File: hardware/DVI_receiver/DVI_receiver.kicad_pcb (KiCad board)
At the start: 4 copper layers, 43 x 25.8 mm, 59 parts, among them J1 HDMI_A, J2 Conn_01x05_Pin, J6 DF12NB(3.0)-30DS-0.5V(51), J7 DF12NB(3.0)-30DS-0.5V(51), Q1 BSS138, U1 TXS0102DCUR, U5 AMS1117-3.3, U8 TFP401

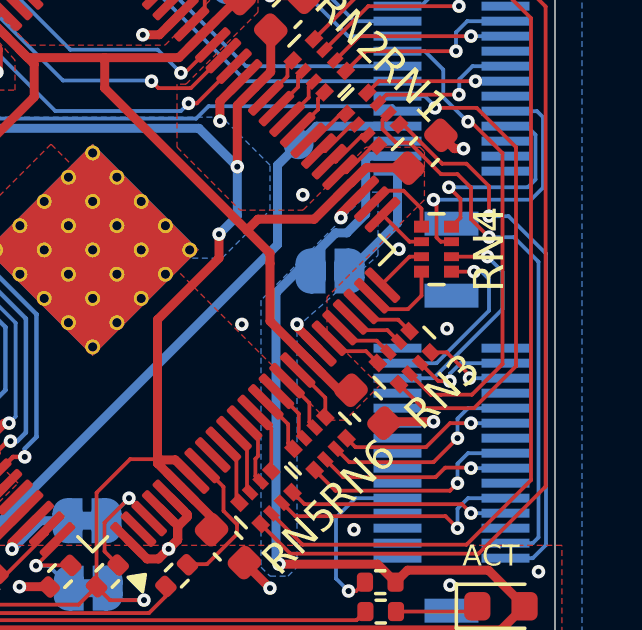
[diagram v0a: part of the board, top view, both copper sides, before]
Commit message: fixed mixup of pins G5/G4 (3rd diff pair ODD) and DE/PCLK (3rd diff pair EVEN), now with correct polarity for diff pairs
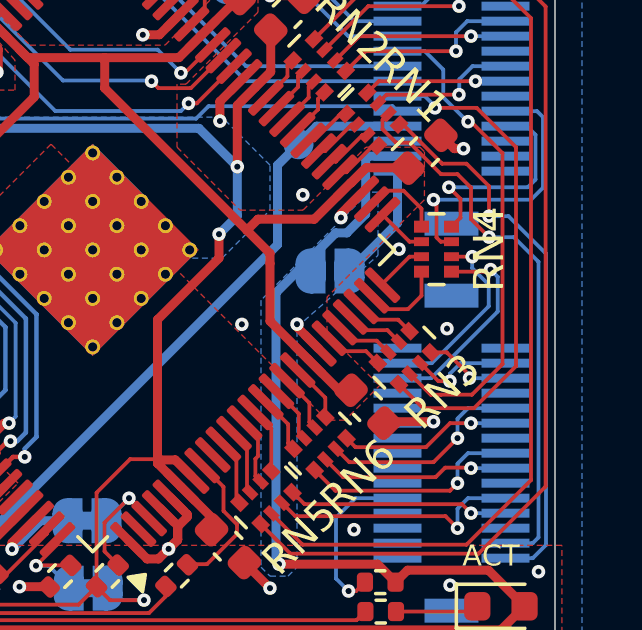
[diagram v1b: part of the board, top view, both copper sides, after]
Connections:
- J6 pad 4: G4 -> G5
- J6 pad 6: G5 -> G4
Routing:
- net G5: track 7.61 -> 6.40 mm
- net G4: track 6.18 -> 7.09 mm
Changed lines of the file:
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@@
 			)
 		)
+		(sheetname "fpga")
+		(sheetfile "fpga.kicad_sch")
 		(attr smd)
 		(fp_line
@@
 			(net 60 "unconnected-(J6-1-Pad2)")
 			(pinfunction "1")
-			(pintype "passive+no_connect")
+			(pintype "passive")
 		)
 		(pad "3" smd rect
@@
 			(size 0.3 1.6)
 			(layers "B.Cu" "B.Paste" "B.Mask")
-			(net 46 "G4")
+			(net 41 "G5")
 			(pinfunction "3")
 			(pintype "passive")
@@
 			(size 0.3 1.6)
 			(layers "B.Cu" "B.Paste" "B.Mask")
-			(net 41 "G5")
+			(net 46 "G4")
 			(pinfunction "5")
 			(pintype "passive")
@@
 	)
 	(segment
-		(start 150.210155 94.319997)
+		(start 149.7 94.319997)
 		(end 149.010155 94.319997)
 		(width 0.127)
@@
 	)
 	(via
-		(at 150.210155 94.319997)
+		(at 149.7 94.319997)
 		(size 0.45)
 		(drill 0.2)
@@
 	)
 	(segment
-		(start 150.710155 96.069998)
-		(end 148.410155 98.369998)
+		(start 150.25 95.975)
+		(end 148.355002 97.869998)
 		(width 0.127)
 		(layer "B.Cu")
@@
 	)
 	(segment
-		(start 150.210155 94.319997)
-		(end 150.710155 94.819996)
+		(start 149.7 94.319997)
+		(end 149.7 94.70191)
 		(width 0.127)
 		(layer "B.Cu")
@@
 	)
 	(segment
-		(start 150.710155 94.819996)
-		(end 150.710155 96.069998)
+		(start 149.7 94.70191)
+		(end 150.25 95.25191)
 		(width 0.127)
 		(layer "B.Cu")
@@
 	)
 	(segment
-		(start 148.410155 98.369998)
-		(end 147.210155 98.369997)
+		(start 148.355002 97.869998)
+		(end 147.210155 97.869998)
+		(width 0.127)
+		(layer "B.Cu")
+		(net 41)
+	)
+	(segment
+		(start 150.25 95.25191)
+		(end 150.25 95.975)
 		(width 0.127)
 		(layer "B.Cu")
@@
 	)
 	(segment
-		(start 149.760156 94.819998)
+		(start 150.241657 94.819998)
 		(end 149.010153 94.819998)
 		(width 0.127)
@@
 		(net 46)
 	)
+	(segment
+		(start 150.311655 94.75)
+		(end 150.241657 94.819998)
+		(width 0.127)
+		(layer "F.Cu")
+		(net 46)
+	)
 	(via
-		(at 149.760156 94.819998)
+		(at 150.311655 94.75)
 		(size 0.45)
 		(drill 0.2)
@@
 	)
 	(segment
-		(start 150.010155 94.819998)
-		(end 150.260155 95.069997)
-		(width 0.127)
-		(layer "B.Cu")
-		(net 46)
-	)
-	(segment
-		(start 149.760156 94.819998)
-		(end 150.010155 94.819998)
+		(start 150.311655 94.75)
+		(end 150.55 94.988345)
 		(width 0.127)
 		(layer "B.Cu")
@@
 	)
 	(segment
-		(start 150.260155 95.069997)
-		(end 150.260155 96.119995)
+		(start 150.55 94.988345)
+		(end 150.55 96.15)
 		(width 0.127)
 		(layer "B.Cu")
@@
 	)
 	(segment
-		(start 150.260155 96.119995)
-		(end 148.510155 97.869997)
+		(start 150.55 96.15)
+		(end 148.330002 98.369998)
 		(width 0.127)
 		(layer "B.Cu")
@@
 	)
 	(segment
-		(start 148.510155 97.869997)
-		(end 147.210155 97.869997)
+		(start 148.330002 98.369998)
+		(end 147.210155 98.369998)
 		(width 0.127)
 		(layer "B.Cu")

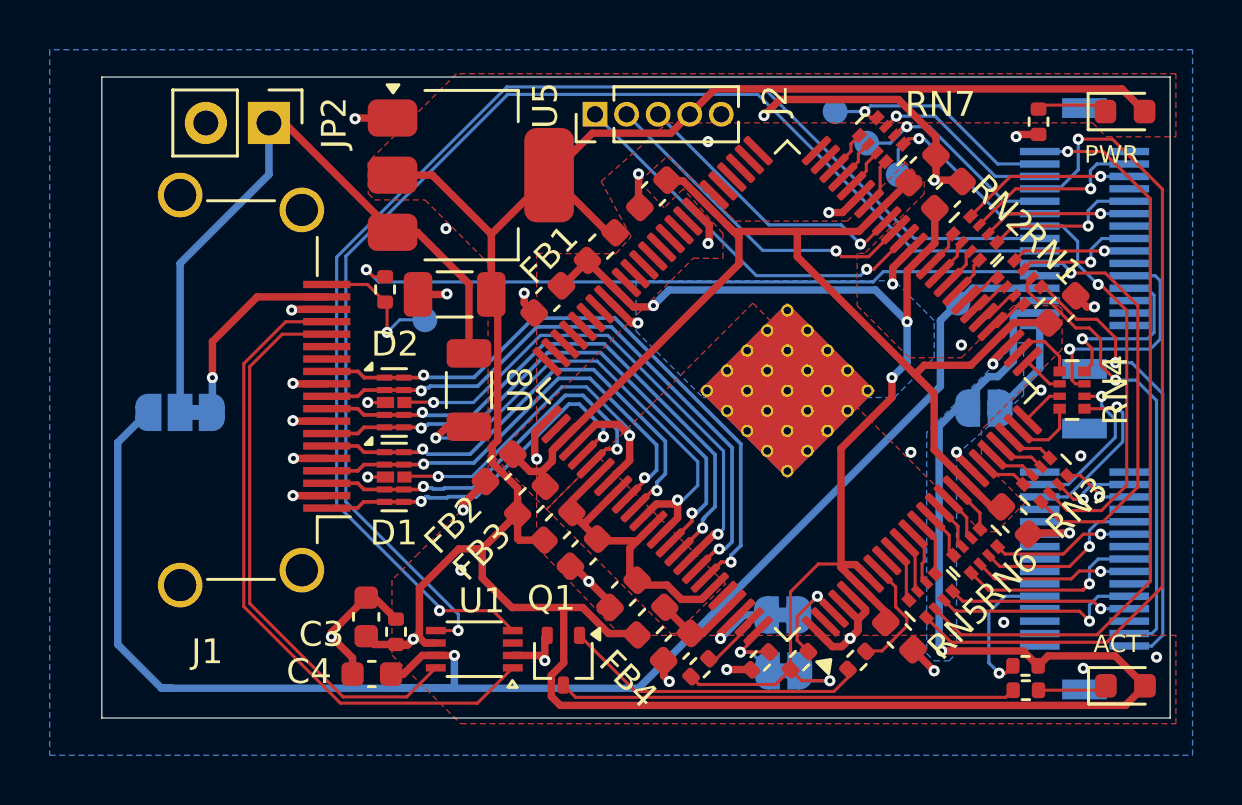
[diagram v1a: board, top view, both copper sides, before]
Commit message: review and update manufacturing constraints (via size, etc.)
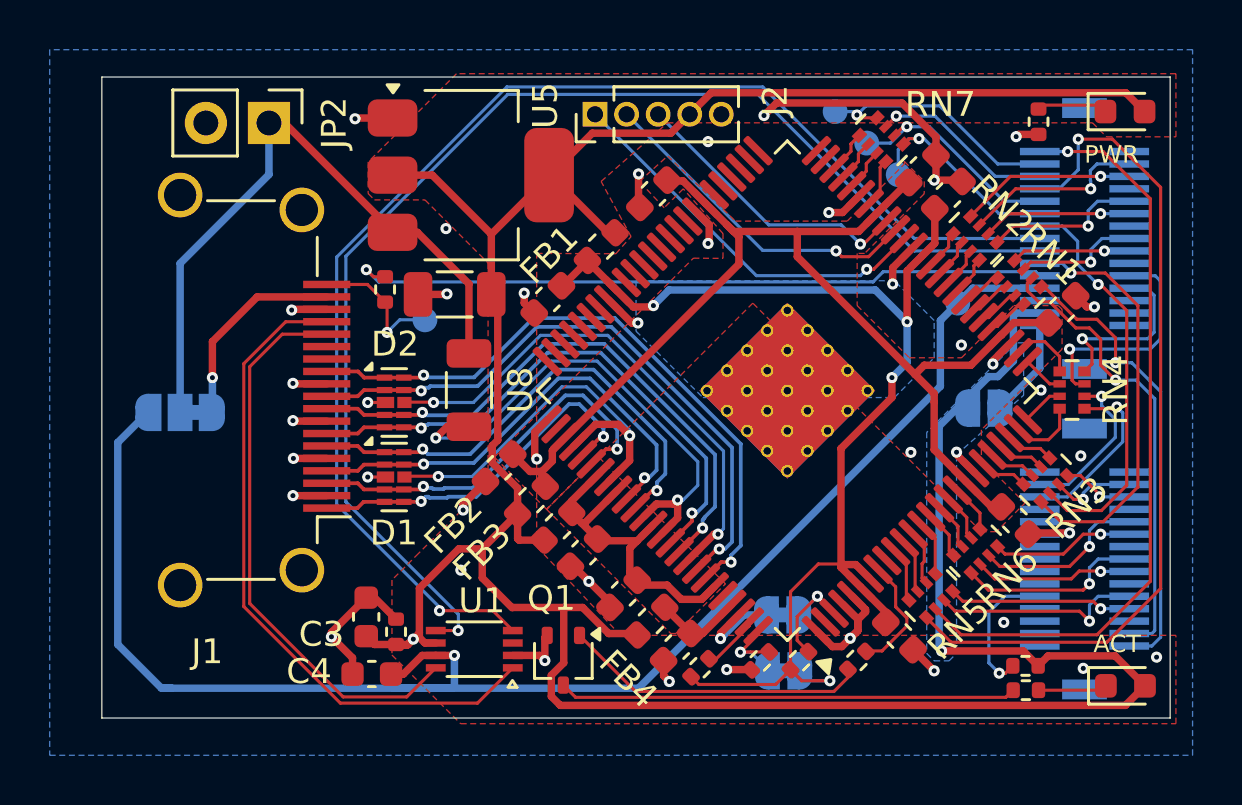
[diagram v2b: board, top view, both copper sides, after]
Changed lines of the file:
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@@
 	)
 	(segment
+		(start 136.110155 83.019996)
+		(end 136.615151 82.515)
+		(width 0.3)
+		(layer "F.Cu")
+		(net 1)
+	)
+	(segment
 		(start 131.27755 99.160215)
 		(end 131.781957 98.655807)
@@
 	)
 	(segment
+		(start 141.665 82.515)
+		(end 143.033162 83.883162)
+		(width 0.3)
+		(layer "F.Cu")
+		(net 1)
+	)
+	(segment
 		(start 124 98.9)
 		(end 124 98.65)
@@
 	)
 	(segment
-		(start 136.755153 82.374998)
-		(end 141.524998 82.374998)
-		(width 0.3)
-		(layer "F.Cu")
-		(net 1)
-	)
-	(segment
 		(start 133.860155 88.169996)
 		(end 133.903277 88.126873)
@@
 	)
 	(segment
-		(start 119.680003 83.119997)
-		(end 119.65 83.15)
+		(start 136.615151 82.515)
+		(end 141.665 82.515)
 		(width 0.3)
 		(layer "F.Cu")
@@
 	)
 	(segment
-		(start 143.033162 83.883162)
-		(end 143.033162 84.62199)
+		(start 119.680003 83.119997)
+		(end 119.65 83.15)
 		(width 0.3)
 		(layer "F.Cu")
@@
 	)
 	(segment
-		(start 136.110155 83.019996)
-		(end 136.755153 82.374998)
-		(width 0.3)
-		(layer "F.Cu")
-		(net 1)
-	)
-	(segment
 		(start 147.160155 83.779996)
 		(end 146.350154 83.779996)
@@
 	)
 	(segment
+		(start 143.033162 83.883162)
+		(end 143.033162 84.62199)
+		(width 0.3)
+		(layer "F.Cu")
+		(net 1)
+	)
+	(segment
 		(start 149.102187 90.719997)
 		(end 148.656171 90.273981)
@@
 	)
 	(segment
-		(start 141.524998 82.374998)
-		(end 143.033162 83.883162)
-		(width 0.3)
-		(layer "F.Cu")
-		(net 1)
-	)
-	(segment
 		(start 141.290155 89.14761)
 		(end 141.290155 89.799998)
@@
 	)
 	(segment
-		(start 140.170156 82.859998)
-		(end 140.42127 83.111112)
+		(start 139.961112 83.111112)
+		(end 140.658377 83.111112)
 		(width 0.127)
 		(layer "F.Cu")
@@
 	)
 	(segment
-		(start 140.42127 83.111112)
-		(end 140.658377 83.111112)
+		(start 139.85 83)
+		(end 139.961112 83.111112)
 		(width 0.127)
 		(layer "F.Cu")
@@
 	)
 	(via
-		(at 140.170156 82.859998)
+		(at 139.85 83)
 		(size 0.45)
 		(drill 0.2)
@@
 	)
 	(segment
-		(start 143.181498 82.631498)
-		(end 145.519997 84.969997)
+		(start 139.709996 82.859996)
+		(end 138.974154 82.859996)
 		(width 0.127)
 		(layer "B.Cu")
@@
 	)
 	(segment
-		(start 140.398656 82.631498)
-		(end 143.181498 82.631498)
+		(start 143.181498 82.631498)
+		(end 145.519997 84.969997)
 		(width 0.127)
 		(layer "B.Cu")
@@
 	)
 	(segment
-		(start 140.170154 82.859996)
-		(end 138.974154 82.859996)
+		(start 145.519997 84.969997)
+		(end 147.210155 84.969997)
 		(width 0.127)
 		(layer "B.Cu")
@@
 	)
 	(segment
-		(start 145.519997 84.969997)
-		(end 147.210155 84.969997)
+		(start 140.218502 82.631498)
+		(end 143.181498 82.631498)
 		(width 0.127)
 		(layer "B.Cu")
@@
 	)
 	(segment
-		(start 140.170156 82.859998)
-		(end 140.170154 82.859996)
+		(start 139.85 83)
+		(end 140.218502 82.631498)
 		(width 0.127)
 		(layer "B.Cu")
@@
 	)
 	(segment
-		(start 140.170156 82.859998)
-		(end 140.398656 82.631498)
+		(start 139.85 83)
+		(end 139.709996 82.859996)
 		(width 0.127)
 		(layer "B.Cu")
@@
 	)
 	(segment
-		(start 152.160154 94.219995)
-		(end 152.160154 103.929996)
+		(start 152.075 104.01515)
+		(end 151.720154 104.369996)
 		(width 0.127)
 		(layer "B.Cu")
@@
 	)
 	(segment
-		(start 152.160154 103.929996)
-		(end 151.720154 104.369996)
+		(start 152.075 94.134841)
+		(end 152.075 104.01515)
 		(width 0.127)
 		(layer "B.Cu")
@@
 	(segment
 		(start 150.910155 92.969996)
-		(end 152.160154 94.219995)
+		(end 152.075 94.134841)
 		(width 0.127)
 		(layer "B.Cu")
@@
 	)
 	(segment
-		(start 150.260155 93.669997)
-		(end 151.090155 93.669997)
+		(start 151.090155 93.669997)
+		(end 151.838 94.417842)
 		(width 0.127)
 		(layer "B.Cu")
@@
 	)
 	(segment
-		(start 151.910155 94.489996)
-		(end 151.910155 103.679997)
+		(start 151.720154 103.869998)
+		(end 150.810155 103.869996)
 		(width 0.127)
 		(layer "B.Cu")
@@
 	)
 	(segment
-		(start 151.720154 103.869998)
-		(end 150.810155 103.869996)
+		(start 150.260155 93.669997)
+		(end 151.090155 93.669997)
 		(width 0.127)
 		(layer "B.Cu")
@@
 	)
 	(segment
-		(start 151.090155 93.669997)
-		(end 151.910155 94.489996)
+		(start 151.838 103.752152)
+		(end 151.720154 103.869998)
 		(width 0.127)
 		(layer "B.Cu")
@@
 	)
 	(segment
-		(start 151.910155 103.679997)
-		(end 151.720154 103.869998)
+		(start 151.838 94.417842)
+		(end 151.838 103.752152)
 		(width 0.127)
 		(layer "B.Cu")
@@
 	)
 	(segment
-		(start 149.910155 104.219996)
-		(end 143.638834 104.219996)
+		(start 143.638834 104.219996)
+		(end 142.649494 103.230656)
 		(width 0.127)
 		(layer "F.Cu")
@@
 	)
 	(segment
-		(start 143.638834 104.219996)
-		(end 142.649494 103.230656)
+		(start 152.075 102.055151)
+		(end 149.910155 104.219996)
 		(width 0.127)
 		(layer "F.Cu")
@@
 	)
 	(segment
-		(start 152.147155 85.981995)
-		(end 152.147155 101.982997)
+		(start 149.910155 104.219996)
+		(end 143.638834 104.219996)
 		(width 0.127)
 		(layer "F.Cu")
@@
 	)
 	(segment
-		(start 150.135155 83.969995)
-		(end 152.147155 85.981995)
+		(start 148.760155 83.969998)
+		(end 150.135155 83.969995)
 		(width 0.127)
 		(layer "F.Cu")
@@
 	)
 	(segment
-		(start 148.760155 83.969998)
-		(end 150.135155 83.969995)
+		(start 152.075 85.90984)
+		(end 152.075 102.055151)
 		(width 0.127)
 		(layer "F.Cu")
@@
 	)
 	(segment
-		(start 152.147155 101.982997)
-		(end 149.910155 104.219996)
+		(start 150.135155 83.969995)
+		(end 152.075 85.90984)
 		(width 0.127)
 		(layer "F.Cu")
@@
 	)
 	(segment
-		(start 151.427655 82.859996)
-		(end 150.517659 81.95)
-		(width 0.3)
-		(layer "F.Cu")
-		(net 137)
-	)
-	(segment
 		(start 127.550155 105.550085)
 		(end 128.05 105.05024)
@@
 	)
 	(segment
+		(start 150.672659 82.105)
+		(end 133.985152 82.105)
+		(width 0.3)
+		(layer "F.Cu")
+		(net 137)
+	)
+	(segment
 		(start 147.145153 105.169997)
 		(end 147.545154 104.769996)
@@
 	)
 	(segment
+		(start 133.985152 82.105)
+		(end 133.120155 82.969997)
+		(width 0.3)
+		(layer "F.Cu")
+		(net 137)
+	)
+	(segment
 		(start 146.545154 104.569997)
 		(end 147.145153 105.169997)
@@
 	)
 	(segment
-		(start 150.517659 81.95)
-		(end 134.140152 81.95)
-		(width 0.3)
-		(layer "F.Cu")
-		(net 137)
-	)
-	(segment
 		(start 125.395154 90.479995)
 		(end 125.135157 90.219998)
@@
 	)
 	(segment
-		(start 134.140152 81.95)
-		(end 133.120155 82.969997)
+		(start 151.427655 82.859996)
+		(end 150.672659 82.105)
 		(width 0.3)
 		(layer "F.Cu")

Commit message: fix R0/R1 mixup
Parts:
- moved G*** 1.43 mm to (121.5, 83.2)
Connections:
- J6 pad 27: R1 -> R0
- J6 pad 29: R0 -> R1
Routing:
- net +5V_OUT: track 62.8 -> 59.2 mm
- net R0: track 18.4 -> 17.6 mm
- net R1: track 18.5 -> 19.3 mm
- net GND: track 120.3 -> 119.6 mm
- net VIO: track 124.7 -> 125.2 mm
- net /fpga/CTL3: track 11.8 -> 12.3 mm
- added copper zone on F.Cu, net VDDIO
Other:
- board text added: "DVI receiver v0.09"
- board text added: "VERSION:"
- board text removed: "DVI Receiver v0.09"

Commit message: fixes for producion and notes
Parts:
- moved TP5 0.46 mm to (141.8, 85.8)
- moved SJ1 0.28 mm to (136.9, 105.7)
- moved TP4 0.28 mm to (140.3, 84.4)
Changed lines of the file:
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@@
 			)
 		)
-		(sheetname "power")
-		(sheetfile "power.kicad_sch")
 		(attr smd)
 		(fp_line
@@
 		(fp_line
 			(start -4.4 3.6)
-			(end 4.4 3.6)
+			(end 2.05 3.6)
 			(stroke
 				(width 0.05)
@@
 		)
 		(fp_line
-			(start 4.4 -3.6)
+			(start 2.05 -3.6)
 			(end -4.4 -3.6)
 			(stroke
@@
 		)
 		(fp_line
-			(start 4.4 3.6)
-			(end 4.4 -3.6)
+			(start 2.05 -3.6)
+			(end 2.05 -2.15)
+			(stroke
+				(width 0.05)
+				(type default)
+			)
+			(layer "F.CrtYd")
+		)
+		(fp_line
+			(start 2.05 -2.15)
+			(end 4.4 -2.15)
+			(stroke
+				(width 0.05)
+				(type default)
+			)
+			(layer "F.CrtYd")
+		)
+		(fp_line
+			(start 2.05 2.15)
+			(end 4.4 2.15)
+			(stroke
+				(width 0.05)
+				(type default)
+			)
+			(layer "F.CrtYd")
+			(net 1915934576)
+		)
+		(fp_line
+			(start 2.05 3.6)
+			(end 2.05 2.15)
+			(stroke
+				(width 0.05)
+				(type default)
+			)
+			(layer "F.CrtYd")
+			(net 1915934576)
+		)
+		(fp_line
+			(start 4.4 2.15)
+			(end 4.4 -2.15)
 			(stroke
 				(width 0.05)
@@
 	(footprint "Jumper:SolderJumper-2_P1.3mm_Bridged_RoundedPad1.0x1.5mm"
 		(layer "B.Cu")
-		(at 136.900154 105.369997)
+		(at 136.900154 105.65)
 		(descr "SMD Solder Jumper, 1x1.5mm, rounded Pads, 0.3mm gap, bridged with 1 copper strip")
 		(tags "net tie solder jumper bridged")
@@
 	(footprint "TestPoint:TestPoint_Pad_D1.0mm"
 		(layer "B.Cu")
-		(at 140.244155 84.129996 -90)
+		(at 140.3 84.4 -90)
 		(descr "SMD pad as test Point, diameter 1.0mm")
 		(tags "test point SMD pad")
@@
 	(footprint "TestPoint:TestPoint_Pad_D1.0mm"
 		(layer "B.Cu")
-		(at 141.514156 85.399997 -90)
+		(at 141.75 85.8 -90)
 		(descr "SMD pad as test Point, diameter 1.0mm")
 		(tags "test point SMD pad")
@@
 	)
 	(segment
-		(start 138.030153 105.769996)
-		(end 137.550154 105.289996)
-		(width 0.127)
-		(layer "B.Cu")
-		(net 29)
-	)
-	(segment
 		(start 141.870156 92.959998)
 		(end 141.870155 91.319997)
@@
 	)
 	(segment
+		(start 137.67015 105.769997)
+		(end 137.550153 105.65)
+		(width 0.127)
+		(layer "B.Cu")
+		(net 29)
+	)
+	(segment
 		(start 138.760155 105.769997)
-		(end 138.030153 105.769996)
+		(end 137.67015 105.769997)
 		(width 0.127)
 		(layer "B.Cu")
@@
 	)
 	(segment
-		(start 147.210155 86.469996)
-		(end 145.769996 86.469996)
+		(start 140.3 84.4)
+		(end 140.930151 84.4)
 		(width 0.127)
 		(layer "B.Cu")
@@
 	)
 	(segment
-		(start 145.769996 86.469996)
-		(end 142.769996 83.469996)
+		(start 140.930151 84.4)
+		(end 141.860155 83.469996)
 		(width 0.127)
 		(layer "B.Cu")
@@
 	)
 	(segment
-		(start 140.244155 84.129996)
-		(end 141.200155 84.129996)
+		(start 147.210155 86.469996)
+		(end 145.769996 86.469996)
 		(width 0.127)
 		(layer "B.Cu")
@@
 	)
 	(segment
-		(start 142.769996 83.469996)
-		(end 141.860155 83.469996)
+		(start 145.769996 86.469996)
+		(end 142.769996 83.469996)
 		(width 0.127)
 		(layer "B.Cu")
@@
 	)
 	(segment
-		(start 141.200155 84.129996)
+		(start 142.769996 83.469996)
 		(end 141.860155 83.469996)
 		(width 0.127)
@@
 	)
 	(segment
-		(start 142.35 83.95)
-		(end 141.948152 83.95)
+		(start 141.75 84.5)
+		(end 141.75 85.8)
 		(width 0.127)
 		(layer "B.Cu")
@@
 	)
 	(segment
-		(start 145.569996 86.969996)
-		(end 147.210155 86.969996)
+		(start 142.3 83.95)
+		(end 141.75 84.5)
 		(width 0.127)
 		(layer "B.Cu")
@@
 	)
 	(segment
-		(start 141.514155 84.383997)
-		(end 141.514156 85.399997)
+		(start 145.569996 86.969996)
+		(end 147.210155 86.969996)
 		(width 0.127)
 		(layer "B.Cu")
@@
 	)
 	(segment
-		(start 141.948152 83.95)
-		(end 141.514155 84.383997)
+		(start 142.35 83.95)
+		(end 142.3 83.95)
 		(width 0.127)
 		(layer "B.Cu")
@@
 	)
 	(segment
-		(start 135.580155 104.619998)
-		(end 136.250155 105.289998)
+		(start 135.160155 104.619996)
+		(end 135.220151 104.619996)
 		(width 0.127)
 		(layer "B.Cu")
@@
 	)
 	(segment
-		(start 135.160155 104.619996)
-		(end 135.580155 104.619998)
+		(start 135.220151 104.619996)
+		(end 136.250155 105.65)
 		(width 0.127)
 		(layer "B.Cu")
@@
 			(pts
 				(xy 135.410155 102.619998) (xy 135.910155 102.119998) (xy 137.860155 102.119998) (xy 138.310155 102.569998)
-				(xy 138.310155 105.919997) (xy 137.960156 106.269997) (xy 135.910155 106.269997) (xy 135.410154 105.769996)
+				(xy 138.310155 106.219997) (xy 137.960156 106.569997) (xy 135.910155 106.569997) (xy 135.410154 106.069996)
 			)
 		)
